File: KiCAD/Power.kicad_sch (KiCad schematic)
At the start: 41 parts, among them J1 Front View, Q3 TIP29A, Q4 2N6594, Q5 2N3906, Q6 MJE34

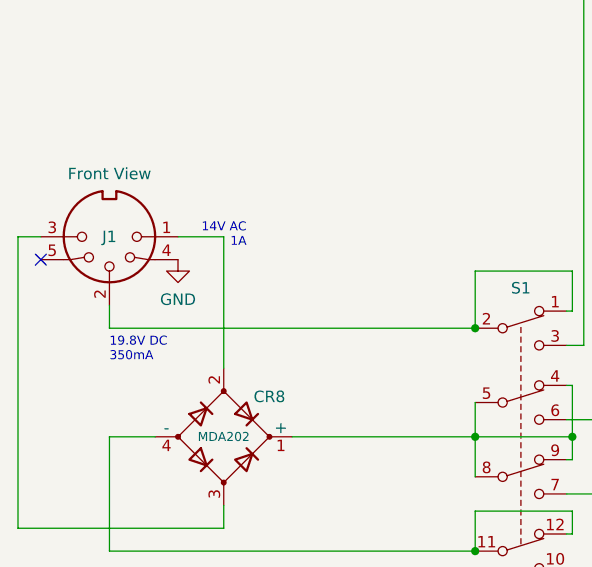
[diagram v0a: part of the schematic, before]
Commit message: New labels file and updated BOM
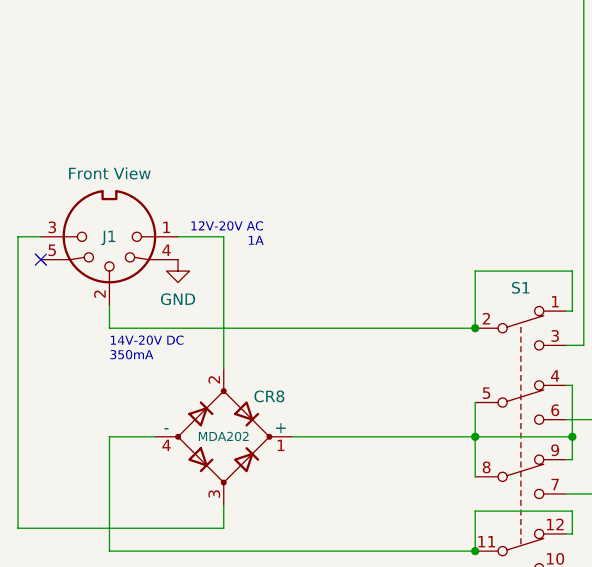
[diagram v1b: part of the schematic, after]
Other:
- note added: "12V-20V AC 1A"
- note added: "14V-20V DC 350mA"
- note removed: "14V AC 1A"
- note removed: "19.8V DC 350mA"
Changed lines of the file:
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@@
     (stroke (width 0) (type default))
   )
-  (text "14V AC\n1A" (at 49.53 81.28 0)
+  (text "12V-20V AC\n1A" (at 51.435 81.28 0)
     (effects (font (size 1 1)) (justify right bottom))
   )
@@
     (effects (font (size 1 1)) (justify left bottom))
   )
-  (text "19.8V DC\n350mA" (at 34.29 93.98 0)
+  (text "14V-20V DC\n350mA" (at 34.29 93.98 0)
     (effects (font (size 1 1)) (justify left bottom))
   )

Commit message: Updated revision to Rev C
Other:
- title: TRS-80 Model I G -> TRS-80 Model I Rev G
